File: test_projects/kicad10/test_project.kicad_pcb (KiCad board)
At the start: 8 copper layers, 57.6 x 50 mm, 91 parts, among them J1 HDMI_A, J2 Conn_01x02_Pin, J3 Barrel_Jack_MountingPin, J4 Conn_01x35_Pin, U1 ASDMB-xxxMHz, U2 ADV7611, U3 LM3880, U4 AP2112K-1.8, U6 RT9742AGJ5F

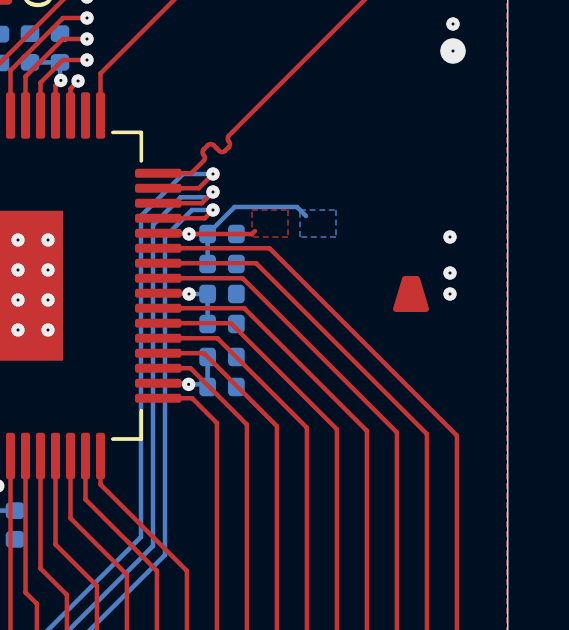
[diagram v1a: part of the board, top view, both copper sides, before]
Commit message: [#92547] test_project: kicad10: Add few more options
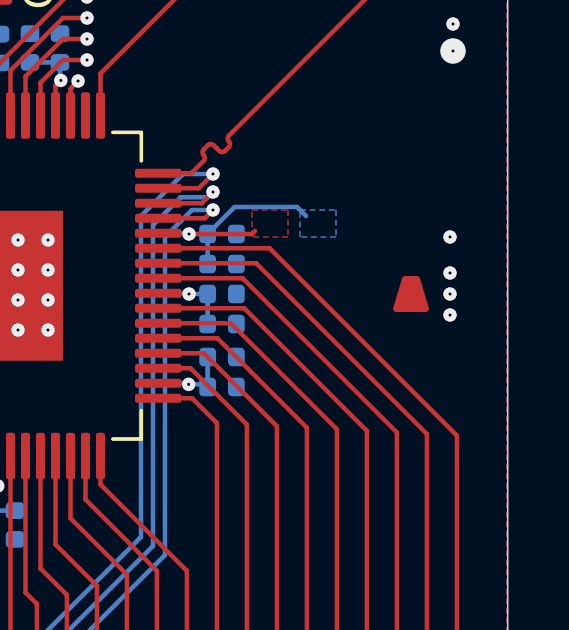
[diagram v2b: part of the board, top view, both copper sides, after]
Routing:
- net +3.3VA: vias 17 -> 18
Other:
- board text added: "Micro Burried Blind Removed annular ring Backdrill, teardrop. .."
- board text removed: "Micro Burried Blind Removed annular ring"
